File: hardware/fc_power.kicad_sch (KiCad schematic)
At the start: 34 parts, among them U3 LMR51430YFDDCR, U4 LMR51430YFDDCR, U6 LP5912-1.8DRVR, U7 LP5912-3.3DRVR

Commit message: OpenAIO: test points TP10-TP30 as LGA position markers (schematic + Base), project files as re-saved by KiCad
Co-Authored-By: Claude Fable 5 <noreply@anthropic.com>
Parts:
- added TP29, TP30: TestPoint, TestPoint:TestPoint_Pad_D1.0mm, symbol Connector:TestPoint
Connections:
- net +3.3V: now also TP29.1
- net GND: now also TP30.1

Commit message: OpenAIO: LGA pins from Stan's marker test points, 30 pads, J90/J91 regenerated and placed
lga_gen.py --from-base reads the marker test points on the Base (position +
net) into its pin table and generates footprints, symbol and interface
sheet; lga_apply.py replaces the markers with J90 at the pattern centre and
J91 on the Core, marks the marker symbols exclude-from-board and adds the
LED_STRIP global label on the root (it now crosses the LGA). Plugin update
assigned all 30 pad nets on both boards.

Co-Authored-By: Claude Fable 5 <noreply@anthropic.com>
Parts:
- removed TP29, TP30: TestPoint, TestPoint:TestPoint_Pad_D1.0mm, symbol Connector:TestPoint
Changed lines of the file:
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@@
-	)
-	(junction
-		(at 252.73 116.84)
-		(diameter 0)
-		(color 0 0 0 0)
 	)
 	(junction
@@
 	(junction
 		(at 191.77 59.69)
-		(diameter 0)
-		(color 0 0 0 0)
-	)
-	(junction
-		(at 252.73 132.08)
 		(diameter 0)
 		(color 0 0 0 0)
@@
 	)
 	(symbol
-		(lib_id "Connector:TestPoint")
-		(at 252.73 116.84 0)
-		(unit 1)
-		(body_style 1)
-		(exclude_from_sim no)
-		(in_bom yes)
-		(on_board yes)
-		(in_pos_files yes)
-		(dnp no)
-		(fields_autoplaced yes)
-		(property "Reference" "TP29"
-			(at 254.635 112.2679 0)
-			(show_name no)
-			(do_not_autoplace no)
-			(effects
-				(font
-					(size 1.27 1.27)
-				)
-				(justify left)
-			)
-		)
-		(property "Value" "TestPoint"
-			(at 254.635 114.8079 0)
-			(show_name no)
-			(do_not_autoplace no)
-			(effects
-				(font
-					(size 1.27 1.27)
-				)
-				(justify left)
-			)
-		)
-		(property "Footprint" "TestPoint:TestPoint_Pad_D1.0mm"
-			(at 257.81 116.84 0)
-			(hide yes)
-			(show_name no)
-			(do_not_autoplace no)
-			(effects
-				(font
-					(size 1.27 1.27)
-				)
-			)
-		)
-		(property "Datasheet" ""
-			(at 257.81 116.84 0)
-			(hide yes)
-			(show_name no)
-			(do_not_autoplace no)
-			(effects
-				(font
-					(size 1.27 1.27)
-				)
-			)
-		)
-		(property "Description" "test point"
-			(at 252.73 116.84 0)
-			(hide yes)
-			(show_name no)
-			(do_not_autoplace no)
-			(effects
-				(font
-					(size 1.27 1.27)
-				)
-			)
-		)
-		(pin "1"
-		)
-		(instances
-			(project "OpenAIO-Base"
-				(path "/fb88b6f9-ee39-4640-a9d4-04a17ceeac64/cdf44e0a-3675-4533-b9f5-78ffc381d2a5"
-					(reference "TP29")
-					(unit 1)
-				)
-			)
-		)
-	)
-	(symbol
 		(lib_id "power:GND")
 		(at 102.87 169.545 0)
@@
 					(unit 1)
 				)
-			)
-		)
-	)
-	(symbol
-		(lib_id "Connector:TestPoint")
-		(at 252.73 132.08 180)
-		(unit 1)
-		(body_style 1)
-		(exclude_from_sim no)
-		(in_bom yes)
-		(on_board yes)
-		(in_pos_files yes)
-		(dnp no)
-		(fields_autoplaced yes)
-		(property "Reference" "TP30"
-			(at 254.635 134.1119 0)
-			(show_name no)
-			(do_not_autoplace no)
-			(effects
-				(font
-					(size 1.27 1.27)
-				)
-				(justify right)
-			)
-		)
-		(property "Value" "TestPoint"
-			(at 254.635 136.6519 0)
-			(show_name no)
-			(do_not_autoplace no)
-			(effects
-				(font
-					(size 1.27 1.27)
-				)
-				(justify right)
-			)
-		)
-		(property "Footprint" "TestPoint:TestPoint_Pad_D1.0mm"
-			(at 247.65 132.08 0)
-			(hide yes)
-			(show_name no)
-			(do_not_autoplace no)
-			(effects
-				(font
-					(size 1.27 1.27)
-				)
-			)
-		)
-		(property "Datasheet" ""
-			(at 247.65 132.08 0)
-			(hide yes)
-			(show_name no)
-			(do_not_autoplace no)
-			(effects
-				(font
-					(size 1.27 1.27)
-				)
-			)
-		)
-		(property "Description" "test point"
-			(at 252.73 132.08 0)
-			(hide yes)
-			(show_name no)
-			(do_not_autoplace no)
-			(effects
-				(font
-					(size 1.27 1.27)
-				)
-			)
-		)
-		(pin "1"
-		)
-		(instances
-			(project "OpenAIO-Base"
-				(path "/fb88b6f9-ee39-4640-a9d4-04a17ceeac64/cdf44e0a-3675-4533-b9f5-78ffc381d2a5"
-					(reference "TP30")
-					(unit 1)
-				)

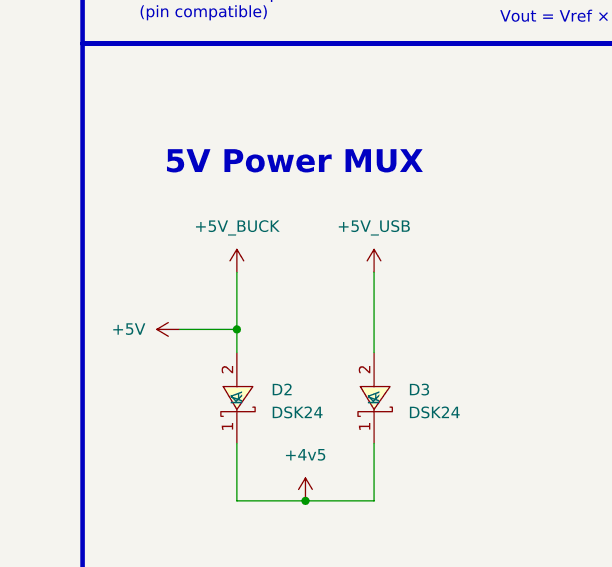
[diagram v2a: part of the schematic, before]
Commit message: OpenAIO: new marker test points TP29 (BUZZER-) and TP30 (+5V) on the Base; lga_apply only excludes the markers it consumed
Co-Authored-By: Claude Fable 5 <noreply@anthropic.com>
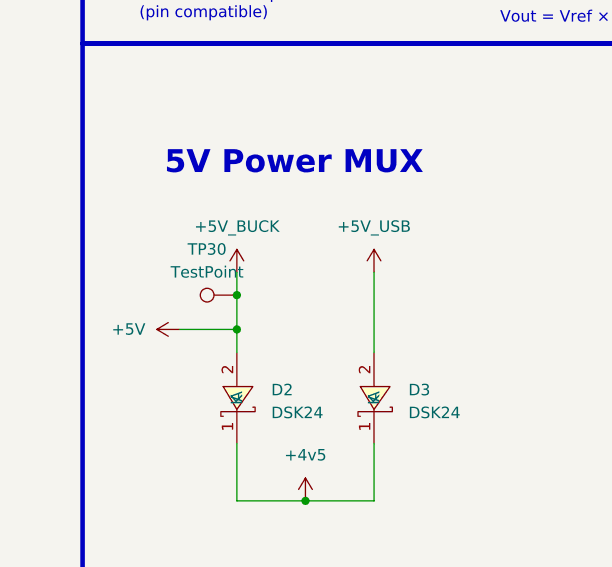
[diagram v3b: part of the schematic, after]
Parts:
- added TP30: TestPoint, TestPoint:TestPoint_Pad_D1.0mm, symbol Connector:TestPoint
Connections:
- net +5V: now also TP30.1
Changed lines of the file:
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@@
 	)
 	(junction
+		(at 31.115 143.51)
+		(diameter 0)
+		(color 0 0 0 0)
+	)
+	(junction
 		(at 31.115 147.32)
 		(diameter 0)
@@
 	(wire
 		(pts
+			(xy 31.115 143.51) (xy 31.115 147.32)
+		)
+		(stroke
+			(width 0)
+			(type default)
+		)
+	)
+	(wire
+		(pts
 			(xy 204.47 71.12) (xy 204.47 72.39)
 		)
@@
 	(wire
 		(pts
-			(xy 31.115 140.97) (xy 31.115 147.32)
+			(xy 31.115 140.97) (xy 31.115 143.51)
 		)
 		(stroke
@@
 					(unit 1)
 				)
+			)
+		)
+	)
+	(symbol
+		(lib_id "Connector:TestPoint")
+		(at 31.115 143.51 90)
+		(unit 1)
+		(body_style 1)
+		(exclude_from_sim no)
+		(in_bom no)
+		(on_board yes)
+		(in_pos_files yes)
+		(dnp no)
+		(fields_autoplaced yes)
+		(property "Reference" "TP30"
+			(at 27.813 138.43 90)
+			(show_name no)
+			(do_not_autoplace no)
+			(effects
+				(font
+					(size 1.27 1.27)
+				)
+			)
+		)
+		(property "Value" "TestPoint"
+			(at 27.813 140.97 90)
+			(show_name no)
+			(do_not_autoplace no)
+			(effects
+				(font
+					(size 1.27 1.27)
+				)
+			)
+		)
+		(property "Footprint" "TestPoint:TestPoint_Pad_D1.0mm"
+			(at 31.115 138.43 0)
+			(hide yes)
+			(show_name no)
+			(do_not_autoplace no)
+			(effects
+				(font
+					(size 1.27 1.27)
+				)
+			)
+		)
+		(property "Datasheet" ""
+			(at 31.115 138.43 0)
+			(hide yes)
+			(show_name no)
+			(do_not_autoplace no)
+			(effects
+				(font
+					(size 1.27 1.27)
+				)
+			)
+		)
+		(property "Description" "test point"
+			(at 31.115 143.51 0)
+			(hide yes)
+			(show_name no)
+			(do_not_autoplace no)
+			(effects
+				(font
+					(size 1.27 1.27)
+				)
+			)
+		)
+		(pin "1"
+		)
+		(instances
+			(project "OpenAIO-Base"
+				(path "/fb88b6f9-ee39-4640-a9d4-04a17ceeac64/cdf44e0a-3675-4533-b9f5-78ffc381d2a5"
+					(reference "TP30")
+					(unit 1)
+				)
